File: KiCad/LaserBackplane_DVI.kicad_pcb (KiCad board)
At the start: 2 copper layers, 69 x 28 mm, 45 parts, among them J1 Curr. Mod., J2 DVI-I, J3 Ld+, J4 Ld-, J5 Pz+, J6 Pz-, J7 Piezo_In, K1 G6AU, Q1 MMBT3904, Q2 2N4401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

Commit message: Cleanup
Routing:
- net LD_short-: track 49.5 -> 46.9 mm

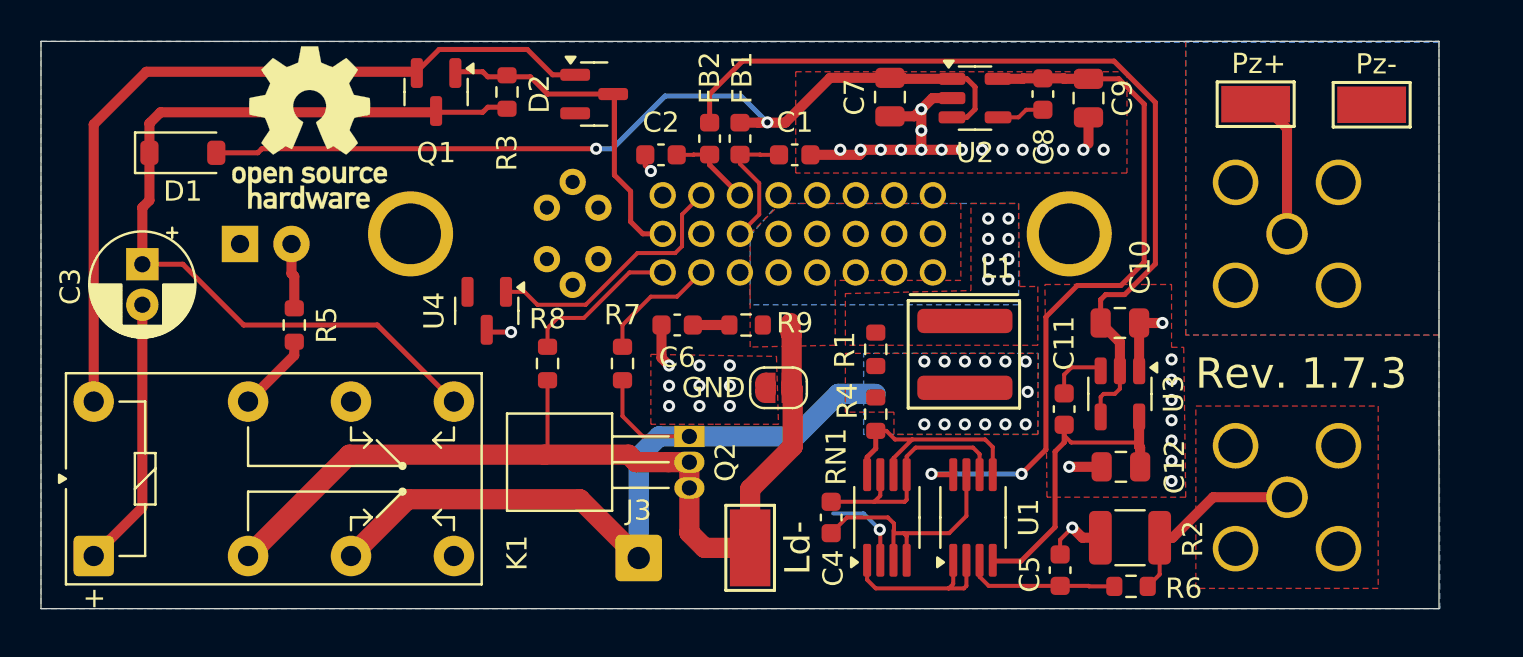
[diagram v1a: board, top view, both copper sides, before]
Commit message: Updated parts
- Swapped 50 ohm resistor for a higher wattage part
- Added bypass capacitors to the current source opamp
- Put all parts on a 0.25 mm grid
- Improved routing
- Removed ground layer keepout below the current source, because there is no significant coupling at 1.6 mm distance
- Added RoHS information
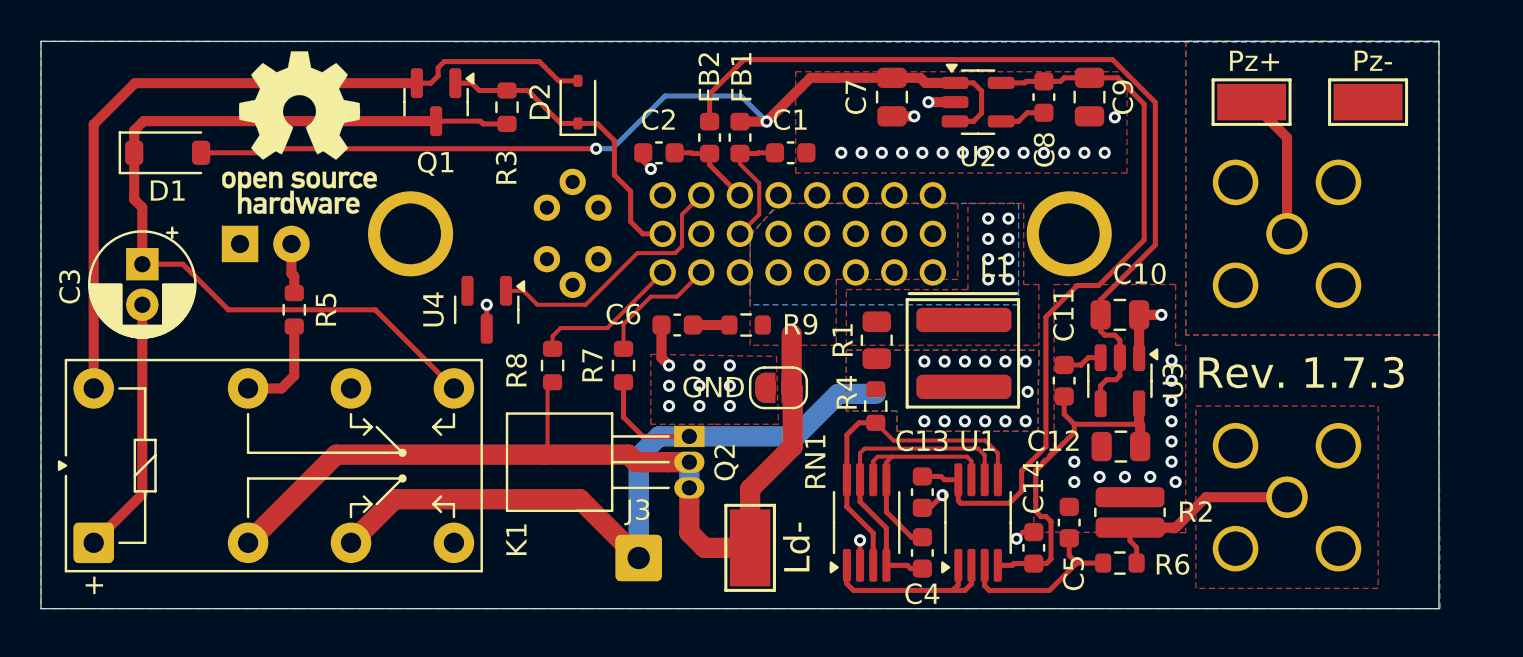
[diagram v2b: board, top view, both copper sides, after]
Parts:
- added C13: 100n, Capacitor_SMD:C_0603_1608Metric, F.Cu at (133.5, 112.2)
- added C14: 100n, Capacitor_SMD:C_0603_1608Metric, F.Cu at (139.0, 115.0)
- D2: value BAT54 -> BAS3010B; footprint Package_TO_SOT_SMD:SOT-23 -> Diode_SMD:D_SOD-323
- R1: footprint Resistor_SMD:R_0603_1608Metric -> Resistor_SMD:R_0805_2012Metric
- R2: footprint Resistor_SMD:R_1210_3225Metric -> Resistor_SMD:R_0612_1632Metric
- U4: value AT21CS11-STXXXX-X -> AT21CS11-STU10-T
- moved C4 4.83 mm to (133.5, 115.2), turned to -90 degrees
- moved C5 2.39 mm to (140.8, 113.8)
- moved C11 1.40 mm to (140.5, 106.8)
- moved R6 1.27 mm to (143.2, 115.8)
- moved R2 1.25 mm to (143.8, 113.2), turned to 90 degrees
- moved RN1 1.03 mm to (130.8, 113.8)
- moved C12 1.00 mm to (143.3, 110.0)
- moved D2 0.89 mm to (116.5, 93.0), turned to 90 degrees
- moved D1 0.75 mm to (96.2, 95.5)
- moved R3 0.75 mm to (113.0, 93.2)
- moved R5 0.75 mm to (102.5, 103.2)
- moved K1 0.65 mm to (92.6, 114.8)
- moved U3 0.65 mm to (143.2, 106.8)
- moved LOGO2 0.56 mm to (102.8, 94.5)
- moved Q1 0.50 mm to (109.5, 93.0)
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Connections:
- C4 pad 1: Net-(RN1C-R3.1) -> Net-(RN1C-R3.2)
- D2 pad 1: Net-(D2-A) -> Relay-
- D2 pad 2: unconnected-(D2-K-Pad2) -> Net-(D2-A)
- RN1 pad 3: Net-(RN1C-R3.1) -> Net-(RN1A-R1.2)
- RN1 pad 4: Net-(RN1C-R3.1) -> Net-(RN1B-R2.2)
- RN1 pad 5: Net-(RN1B-R2.2) -> Net-(RN1C-R3.2)
- RN1 pad 6: Net-(RN1A-R1.2) -> Net-(RN1C-R3.2)
- U1 pad 7: Net-(RN1C-R3.1) -> Net-(RN1C-R3.2)
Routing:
- net GND: track 30.6 -> 13.4 mm, vias 38 -> 44
- net Net-(RN1C-R3.1): track 12.9 -> 0.00 mm
- net Net-(RN1C-R3.2): track 0.00 -> 12.0 mm
- net Net-(RN1A-R1.2): track 11.9 -> 16.6 mm
- net Relay-: track 19.4 -> 15.2 mm
- net Net-(RN1B-R2.2): track 12.3 -> 15.5 mm
- net -5V: track 15.8 -> 17.6 mm
- net Net-(D4-A): track 3.81 -> 2.48 mm
- net Net-(U1A-+): track 7.66 -> 8.90 mm
- net Net-(K1-Pad21): track 3.97 -> 4.97 mm
- net Net-(U3-BYP): track 2.87 -> 1.95 mm
- net +5V: track 35.3 -> 36.2 mm, vias 2 -> 0
- net LD_short-: track 46.9 -> 46.1 mm
- net Net-(RN1A-R1.1): track 8.76 -> 9.60 mm
- net -12V: track 43.4 -> 42.7 mm
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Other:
- board text added: "Designed on a 0.25 mm grid"

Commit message: Bump version to 1.7.4
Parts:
- moved LOGO1 1.70 mm to (144.2, 109.0)
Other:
- board text added: "LaserBackplane v1.7.4 Design: T. Preuschoff, P. Baus Date: 2024-05 https://github.com/TU-Darmstadt-APQ/ Laser_Backplane_DVI"
- board text added: "Rev. 1.7.4"
- board text removed: "LaserBackplane Tilman Preuschoff 11/2023 Rev 1.7.3"
- board text removed: "Rev. 1.7.3"
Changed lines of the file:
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@@
 	(title_block
 		(title "Laser Backplane Diode DVI")
-		(date "2023-11-15")
-		(rev "1.7.3")
+		(date "2024-05-14")
+		(rev "1.7.4")
 		(company "APQ")
 		(comment 1 "Tilman Preuschoff & Patrick Baus")
@@
 		(tags "SOD-323")
 		(property "Reference" "D2"
-			(at 0 -1.85 270)
+			(at 0 -1.85 -90)
 			(layer "F.SilkS")
 			(effects
@@
 		)
 		(property "Value" "BAS3010B"
-			(at 0.1 1.9 270)
+			(at 0.1 1.9 -90)
 			(layer "F.Fab")
 			(effects
@@
 		)
 		(property "MFN" "Infineon Technologies"
-			(at 0 0 270)
+			(at 0 0 -90)
 			(layer "F.Fab")
 			(hide yes)
@@
 		)
 		(property "Note" "Use a low Vf Schottky"
-			(at 0 0 270)
+			(at 0 0 -90)
 			(layer "F.Fab")
 			(hide yes)
@@
 		)
 		(property "PN" "BAS3010B03WE6327HTSA1"
-			(at 0 0 270)
+			(at 0 0 -90)
 			(layer "F.Fab")
 			(hide yes)
@@
 		)
 		(fp_text user "${REFERENCE}"
-			(at 0 -1.85 270)
+			(at 0 -1.85 -90)
 			(layer "F.Fab")
 			(effects
@@
 		(tags "Omron G6A Relay DPDT")
 		(property "Reference" "K1"
-			(at 0.15 20.9 270)
+			(at 0.15 20.9 -90)
 			(layer "F.SilkS")
 			(effects
@@
 		)
 		(property "Value" "G6AU"
-			(at 3.81 20.5 270)
+			(at 3.81 20.5 -90)
 			(layer "F.Fab")
 			(effects
@@
 		)
 		(property "MFN" "Omron"
-			(at 0 0 270)
+			(at 0 0 -90)
 			(layer "F.Fab")
 			(hide yes)
@@
 		)
 		(property "PN" "G6AU-274P-ST-US-DC9"
-			(at 0 0 270)
+			(at 0 0 -90)
 			(layer "F.Fab")
 			(hide yes)
@@
 		)
 		(fp_text user "${REFERENCE}"
-			(at 3.81 8.89 360)
+			(at 3.81 8.89 0)
 			(layer "F.Fab")
 			(effects
@@
 		)
 		(property "Value" "49.9"
-			(at 0 2.65 270)
+			(at 0 2.65 -90)
 			(layer "F.Fab")
 			(effects
@@
 		)
 		(property "Config" "+curr_mod"
-			(at 0 0 270)
+			(at 0 0 -90)
 			(layer "F.Fab")
 			(hide yes)
@@
 		)
 		(property "MFN" "ROHM Semiconductor"
-			(at 0 0 270)
+			(at 0 0 -90)
 			(layer "F.Fab")
 			(hide yes)
@@
 		)
 		(property "PN" "LTR18EZPF49R9"
-			(at 0 0 270)
+			(at 0 0 -90)
 			(layer "F.Fab")
 			(hide yes)
@@
 		)
 		(property "variant" "curr_mod"
-			(at 0 0 270)
+			(at 0 0 -90)
 			(layer "F.Fab")
 			(hide yes)
@@
 		)
 		(fp_text user "${REFERENCE}"
-			(at 0 0 270)
+			(at 0 0 -90)
 			(layer "F.Fab")
 			(effects
@@
 		(tags "capacitor")
 		(property "Reference" "C14"
-			(at 3 0 270)
+			(at 3 0 -90)
 			(layer "F.SilkS")
 			(effects
@@
 		)
 		(property "Value" "100n"
-			(at 0 1.43 270)
+			(at 0 1.43 -90)
 			(layer "F.Fab")
 			(effects
@@
 		)
 		(fp_text user "${REFERENCE}"
-			(at 0 0 270)
+			(at 0 0 -90)
 			(layer "F.Fab")
 			(effects
@@
 	(footprint "custom:APQ-Logo_small"
 		(layer "B.Cu")
-		(at 144.2 110.7)
+		(at 144.2 109)
 		(property "Reference" "LOGO1"
 			(at 0 0 0)
@@
 		(layer "Edge.Cuts")
 	)
-	(gr_text "LaserBackplane\nTilman Preuschoff\n11/2023 Rev 1.7.3"
+	(gr_text "LaserBackplane v1.7.4\nDesign: T. Preuschoff, P. Baus\nDate: 2024-05\nhttps://github.com/TU-Darmstadt-APQ/\nLaser_Backplane_DVI"
 		(at 146.6 113.95 0)
 		(layer "B.SilkS")
 		(effects
 			(font
-				(size 1 1)
+				(size 0.8 0.8)
 				(thickness 0.15)
 			)
@@
 		)
 	)
-	(gr_text "Rev. 1.7.3"
+	(gr_text "Rev. 1.7.4"
 		(at 152.2 106.4 0)
 		(layer "F.SilkS")

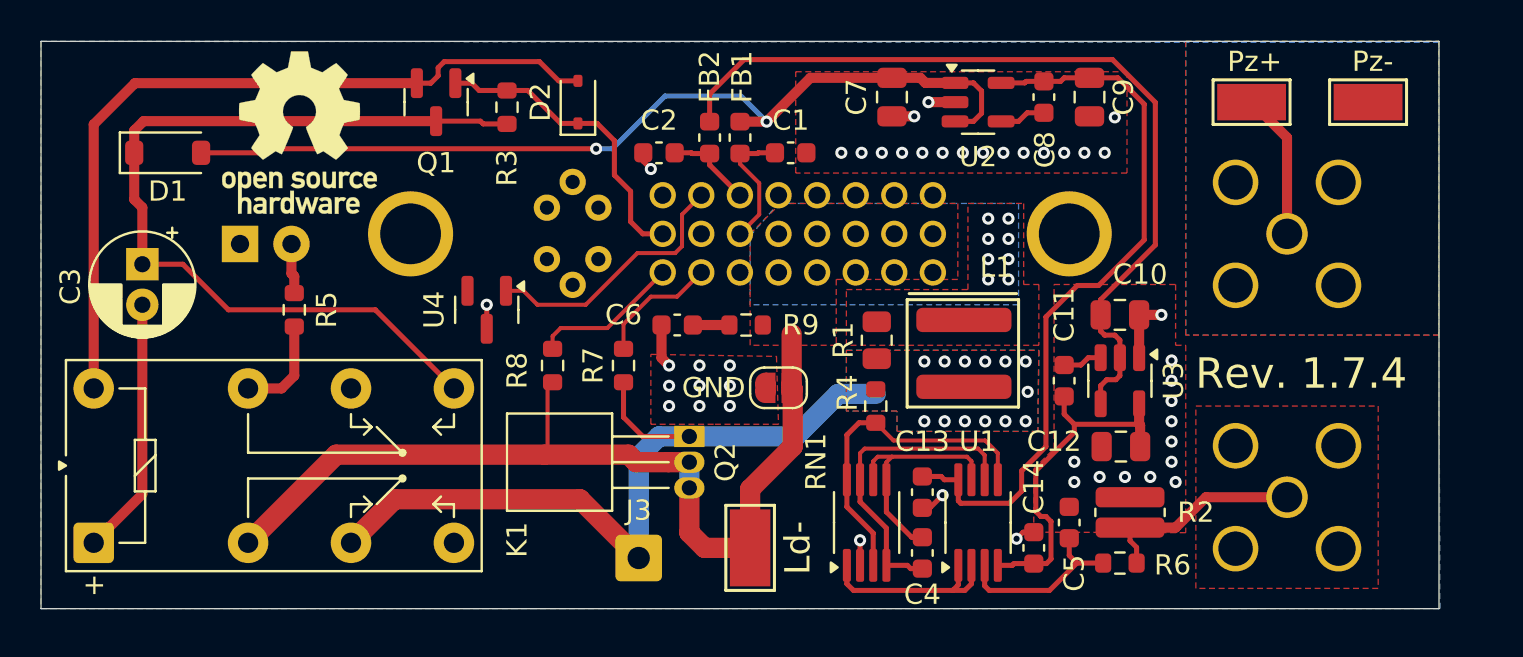
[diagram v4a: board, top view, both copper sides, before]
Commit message: 1.7.4 (#5)
* Add chamfer to corners

* Change line with of the part dimentsions to 0.1 mm

* Add teardrops

* Added peizo driver high voltage warning

* Add PCBA variant

* Cleaned up labels

* Create individual gerber files for all variants to make sure DNP parts are not included in the mask layer
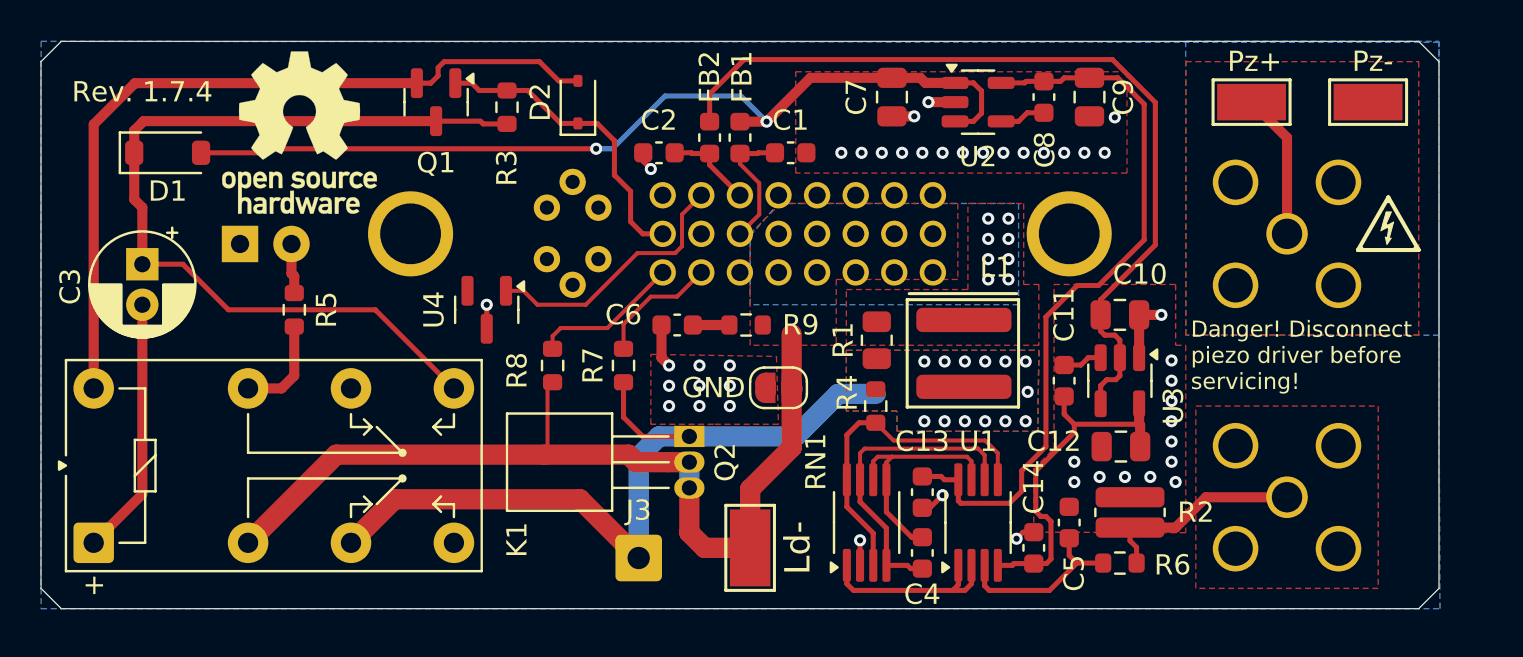
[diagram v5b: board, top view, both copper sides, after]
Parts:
- added SYM1: SYM_Flash_Small, custom:Symbol_HighVoltage_Triangle_3x3mm, F.Cu at (156.5, 99.0)
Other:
- outline, holes or cut-outs redrawn
- board text added: "Danger! Disconnect piezo driver before servicing!"

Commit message: Added SMP connector
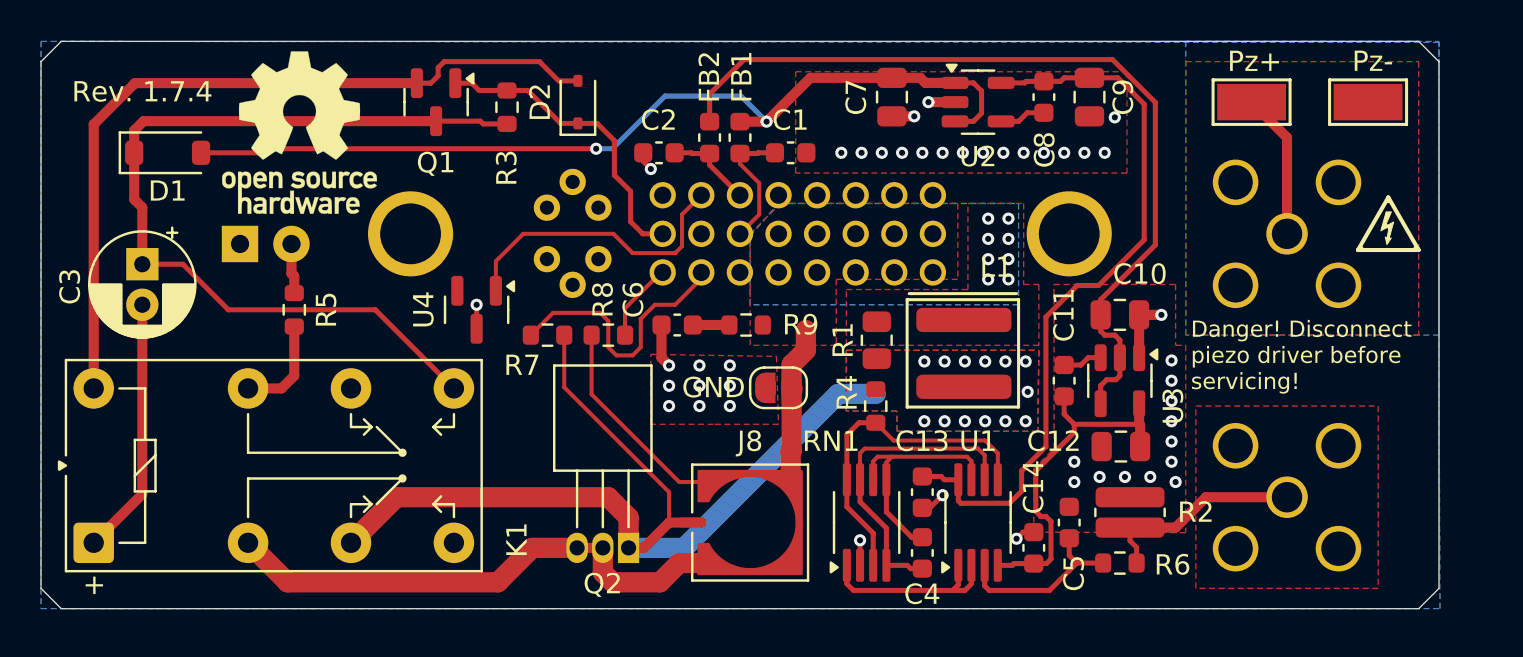
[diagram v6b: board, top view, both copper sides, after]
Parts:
- removed J3: Ld+, Connector_Wire:SolderWire-0.5sqmm_1x01_D0.9mm_OD2.3mm
- removed J4: Ld-, TestPoint:TestPoint_Keystone_5019_Minature
- added J8: Conn_Coaxial, custom:SMP_TE_CONSMP001-SMD-G-T_Vertical, F.Cu at (125.0, 113.8)
- moved Q2 6.26 mm to (119.0, 115.0), turned to 180 degrees
- moved R7 4.04 mm to (115.0, 104.5), turned to 180 degrees
- moved R8 3.13 mm to (118.0, 104.5), turned to 180 degrees
- moved U4 0.50 mm to (111.5, 103.2)
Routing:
- net Curr_Mod: track 39.6 -> 47.4 mm
- net V_diode+: track 6.12 -> 13.2 mm
- net V_diode-: track 7.37 -> 3.92 mm
- net LD_short-: track 46.1 -> 44.5 mm
- net Net-(J2-DDCIO): track 13.1 -> 14.7 mm

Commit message: Bump version to 1.8.0
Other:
- board text added: "LaserBackplane v1.8.0 Design: T. Preuschoff, P. Baus Date: 2024-05 https://github.com/TU-Darmstadt-APQ/ Laser_Backplane_DVI"
- board text added: "Rev. 1.8.0"
- board text removed: "LaserBackplane v1.7.4 Design: T. Preuschoff, P. Baus Date: 2024-05 https://github.com/TU-Darmstadt-APQ/ Laser_Backplane_DVI"
- board text removed: "Rev. 1.7.4"
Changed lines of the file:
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@@
 	(title_block
 		(title "Laser Backplane Diode DVI")
-		(date "2024-05-14")
-		(rev "1.7.4")
+		(date "2024-05-15")
+		(rev "1.8.0")
 		(company "APQ")
 		(comment 1 "Tilman Preuschoff & Patrick Baus")
@@
 		(layer "Edge.Cuts")
 	)
-	(gr_text "LaserBackplane v1.7.4\nDesign: T. Preuschoff, P. Baus\nDate: 2024-05\nhttps://github.com/TU-Darmstadt-APQ/\nLaser_Backplane_DVI"
+	(gr_text "LaserBackplane v1.8.0\nDesign: T. Preuschoff, P. Baus\nDate: 2024-05\nhttps://github.com/TU-Darmstadt-APQ/\nLaser_Backplane_DVI"
 		(at 146.6 113.95 0)
 		(layer "B.SilkS")
@@
 		)
 	)
-	(gr_text "Rev. 1.7.4"
+	(gr_text "Rev. 1.8.0"
 		(at 95 92.5 0)
 		(layer "F.SilkS")

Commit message: Updated DVI connector footprint
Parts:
- J2: footprint custom:DVI-I_Conn_Link_CDVI-F29VDG1-P1 -> custom:DVI-I_Conn-Link_CDVI-F29VDG1-P1_Vertical
- moved J2 10.6 mm to (114.6, 103.4)
